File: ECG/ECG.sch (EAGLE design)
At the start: 32 parts, among them J1 TC2030-CTX-NL, U1 BGM111-VISUAL-A, U2 AD8232

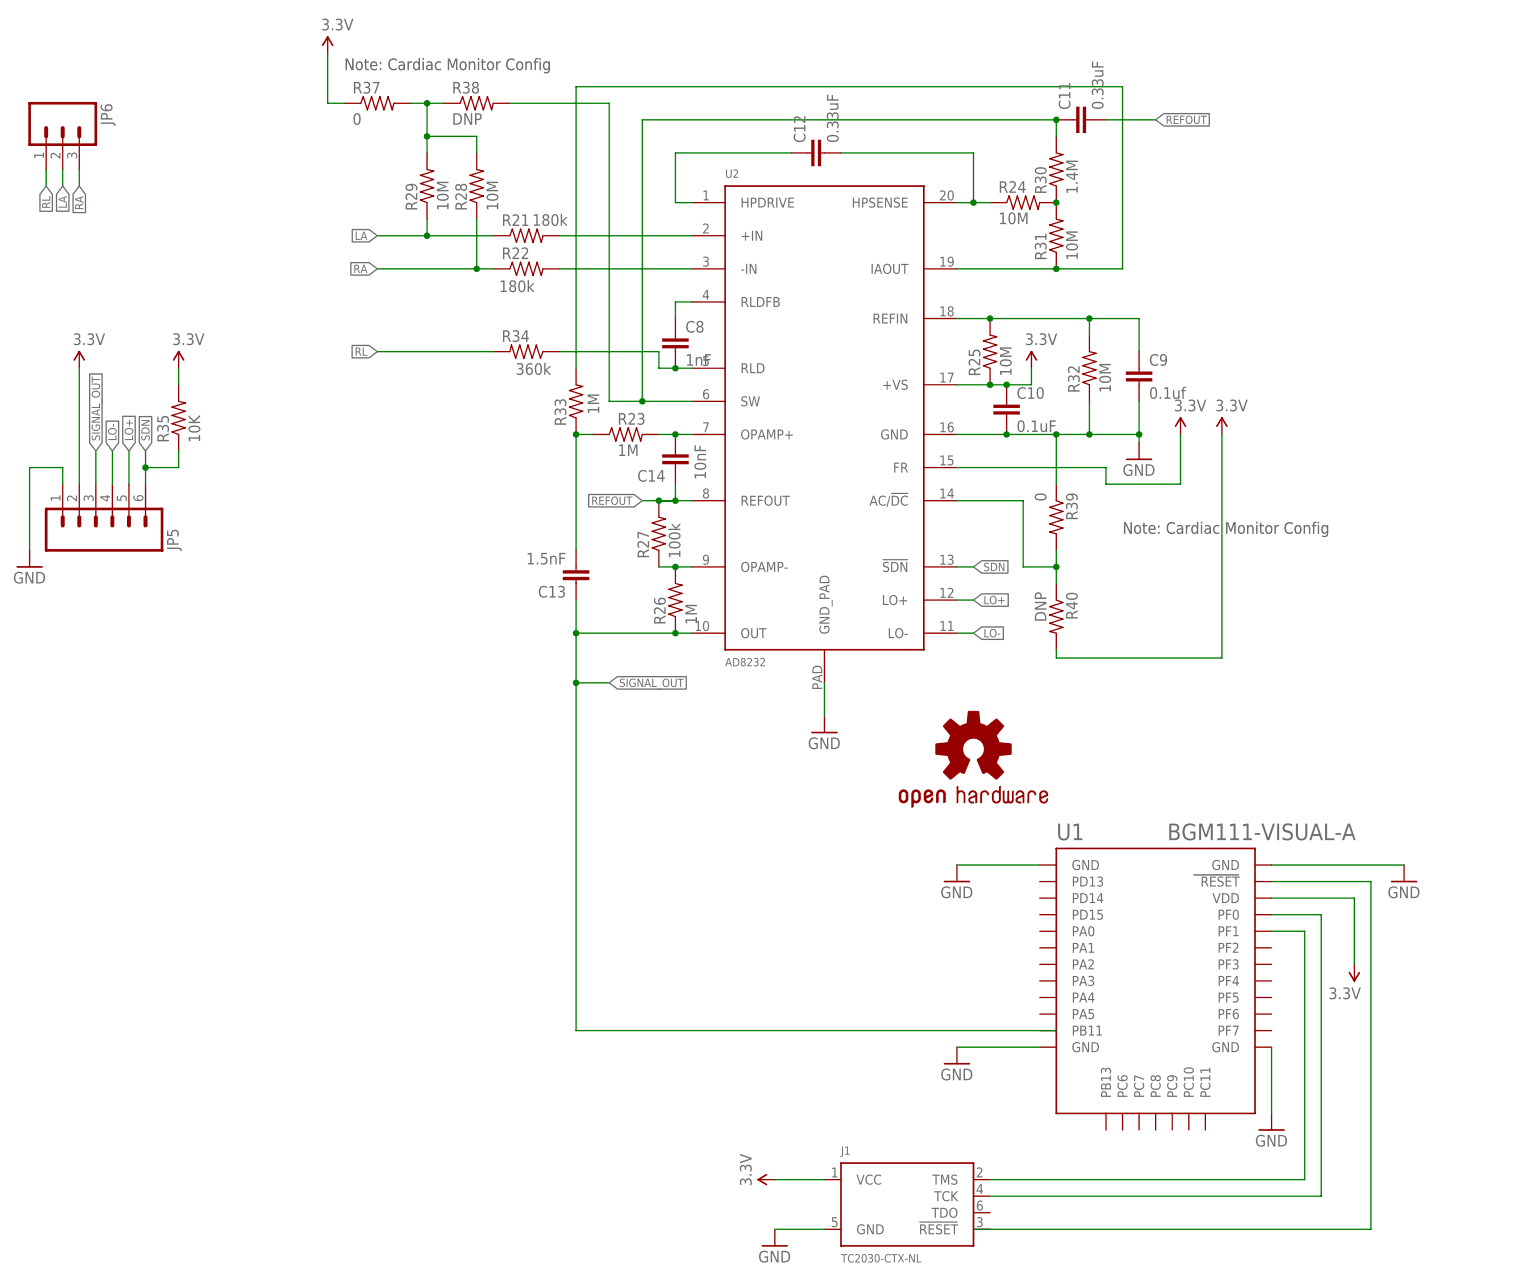
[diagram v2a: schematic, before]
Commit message: Added Batteryholder and snap connectors for RA,LA
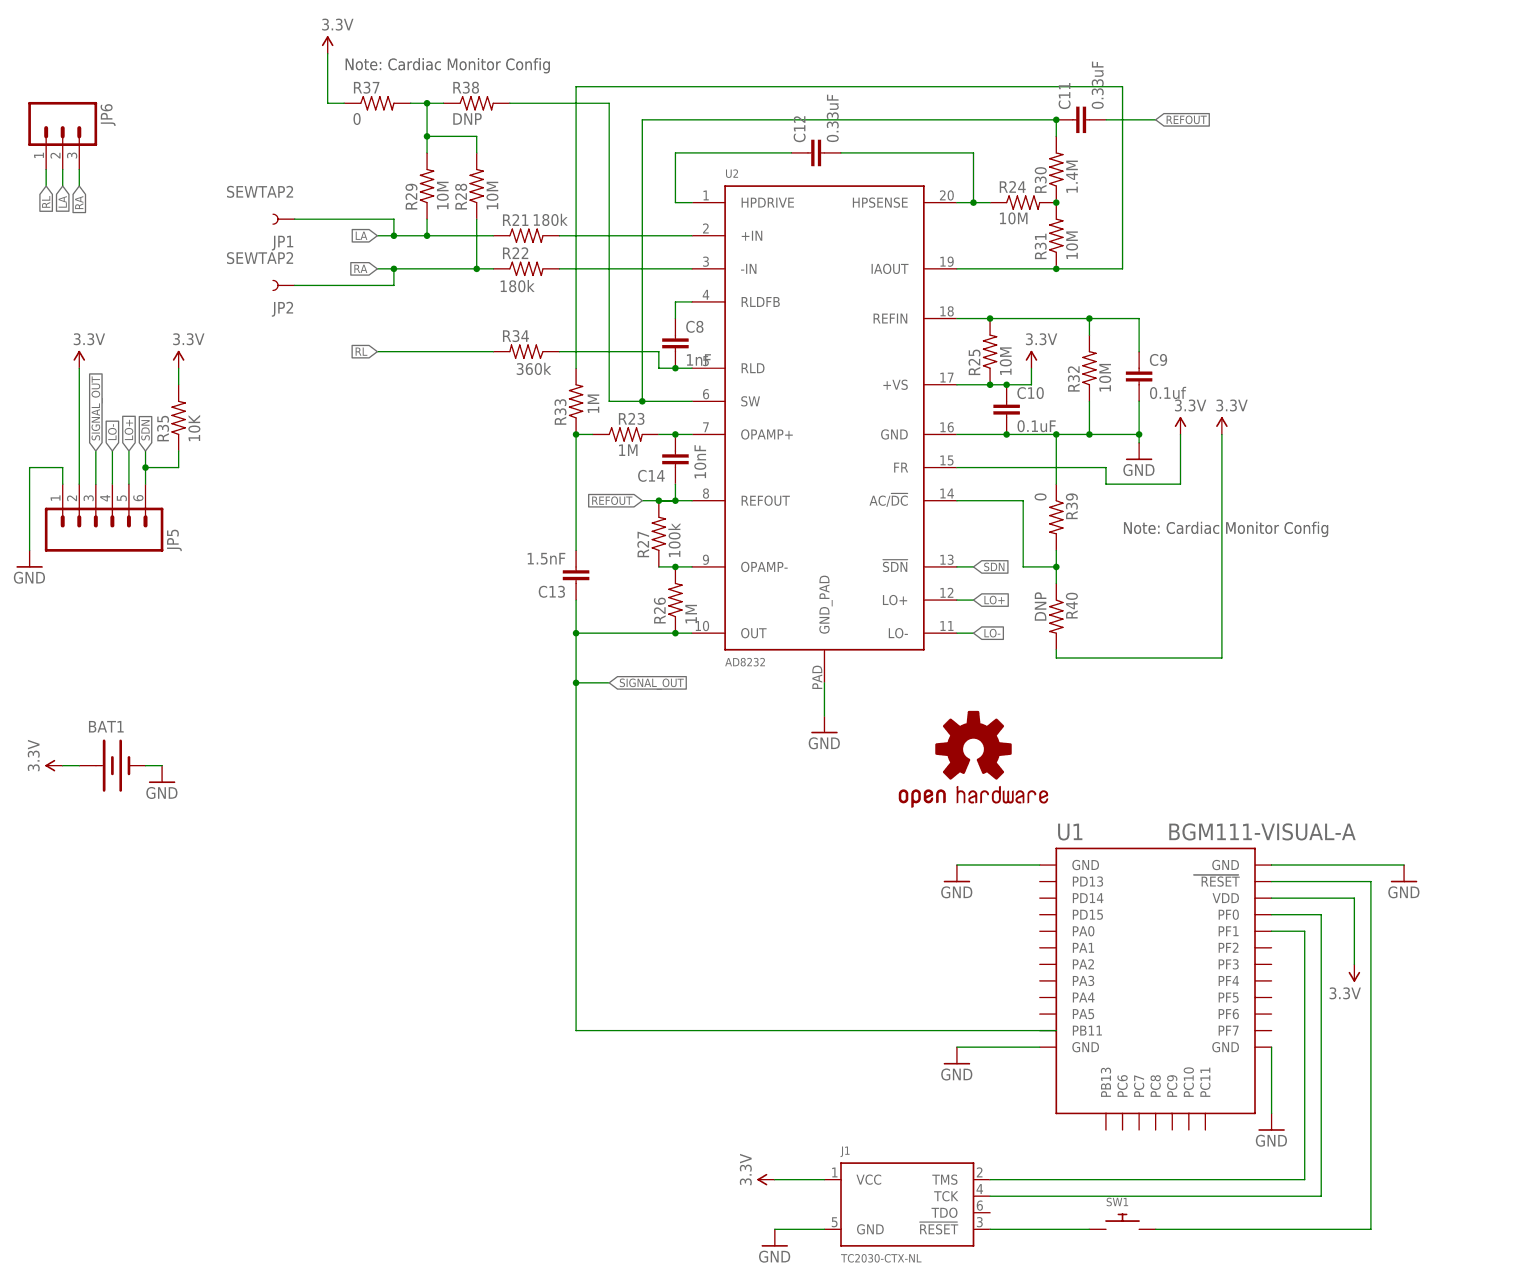
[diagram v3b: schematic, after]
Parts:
- added BAT1: (no value), SparkFun-Electromechanical:BATTERY20SMD
- added JP1, JP2: SEWTAP2, LilyPad-Wearables:SEWTAP2
- added SW1: (no value), adafruit:SWITCH_PUSHBUTTONSOFTTOUCHSMD_SJ
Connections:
- new net N$1: J1.!RESET, SW1.P$1
- net 3.3V: now also BAT1.+
- net GND: now also BAT1.-
- net LA: now also JP1.1
- net N$2: now also SW1.P$2
- net RA: now also JP2.1
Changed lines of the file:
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@@
 <part name="J1" library="tag_connector" deviceset="TC2030-CTX" device="-NL"/>
 <part name="SUPPLY1" library="SparkFun-Aesthetics" deviceset="3.3V" device=""/>
+<part name="BAT1" library="SparkFun-Electromechanical" deviceset="BATTERY" device="20SMD"/>
+<part name="GND9" library="SparkFun-Aesthetics" deviceset="GND" device=""/>
+<part name="SUPPLY3" library="SparkFun-Aesthetics" deviceset="3.3V" device=""/>
+<part name="JP1" library="LilyPad-Wearables" deviceset="SEWTAP" device="2"/>
+<part name="JP2" library="LilyPad-Wearables" deviceset="SEWTAP" device="2"/>
+<part name="SW1" library="adafruit" deviceset="SWITCH_PUSHBUTTON" device="SOFTTOUCHSMD_SJ"/>
 </parts>
 <sheets>
@@
 <instance part="J1" gate="G$1" x="139.7" y="-109.22"/>
 <instance part="SUPPLY1" gate="G$1" x="119.38" y="-106.68" rot="R90"/>
+<instance part="BAT1" gate="G$1" x="17.78" y="-43.18"/>
+<instance part="GND9" gate="1" x="25.4" y="-45.72"/>
+<instance part="SUPPLY3" gate="G$1" x="10.16" y="-43.18" rot="R90"/>
+<instance part="JP1" gate="G$1" x="43.18" y="40.64" rot="R180"/>
+<instance part="JP2" gate="G$1" x="43.18" y="30.48" rot="R180"/>
+<instance part="SW1" gate="G$1" x="172.72" y="-114.3"/>
 </instances>
 <busses>
@@
 <wire x1="119.38" y1="-114.3" x2="127" y2="-114.3" width="0.1524" layer="91"/>
 </segment>
+<segment>
+<pinref part="BAT1" gate="G$1" pin="-"/>
+<pinref part="GND9" gate="1" pin="GND"/>
+<wire x1="22.86" y1="-43.18" x2="25.4" y2="-43.18" width="0.1524" layer="91"/>
+</segment>
 </net>
 <net name="N$12" class="0">
@@
 <wire x1="76.2" y1="38.1" x2="66.04" y2="38.1" width="0.1524" layer="91"/>
 <pinref part="R29" gate="G$1" pin="1"/>
-<wire x1="66.04" y1="38.1" x2="58.42" y2="38.1" width="0.1524" layer="91"/>
+<wire x1="66.04" y1="38.1" x2="60.96" y2="38.1" width="0.1524" layer="91"/>
+<wire x1="60.96" y1="38.1" x2="58.42" y2="38.1" width="0.1524" layer="91"/>
 <wire x1="66.04" y1="40.64" x2="66.04" y2="38.1" width="0.1524" layer="91"/>
 <junction x="66.04" y="38.1"/>
 <label x="58.42" y="38.1" size="1.27" layer="95" rot="R180" xref="yes"/>
+<pinref part="JP1" gate="G$1" pin="1"/>
+<wire x1="45.72" y1="40.64" x2="60.96" y2="40.64" width="0.1524" layer="91"/>
+<wire x1="60.96" y1="40.64" x2="60.96" y2="38.1" width="0.1524" layer="91"/>
+<junction x="60.96" y="38.1"/>
 </segment>
 <segment>
@@
 <wire x1="76.2" y1="33.02" x2="73.66" y2="33.02" width="0.1524" layer="91"/>
 <pinref part="R28" gate="G$1" pin="1"/>
-<wire x1="73.66" y1="33.02" x2="58.42" y2="33.02" width="0.1524" layer="91"/>
+<wire x1="73.66" y1="33.02" x2="60.96" y2="33.02" width="0.1524" layer="91"/>
+<wire x1="60.96" y1="33.02" x2="58.42" y2="33.02" width="0.1524" layer="91"/>
 <wire x1="73.66" y1="40.64" x2="73.66" y2="33.02" width="0.1524" layer="91"/>
 <junction x="73.66" y="33.02"/>
 <label x="58.42" y="33.02" size="1.27" layer="95" rot="R180" xref="yes"/>
+<pinref part="JP2" gate="G$1" pin="1"/>
+<wire x1="45.72" y1="30.48" x2="60.96" y2="30.48" width="0.1524" layer="91"/>
+<wire x1="60.96" y1="30.48" x2="60.96" y2="33.02" width="0.1524" layer="91"/>
+<junction x="60.96" y="33.02"/>
 </segment>
 <segment>
@@
 <pinref part="SUPPLY2" gate="G$1" pin="3.3V"/>
 </segment>
+<segment>
+<pinref part="SUPPLY3" gate="G$1" pin="3.3V"/>
+<pinref part="BAT1" gate="G$1" pin="+"/>
+<wire x1="10.16" y1="-43.18" x2="12.7" y2="-43.18" width="0.1524" layer="91"/>
+</segment>
 </net>
 <net name="LO+" class="0">
@@
 </segment>
 </net>
+<net name="N$1" class="0">
+<segment>
+<pinref part="J1" gate="G$1" pin="!RESET"/>
+<pinref part="SW1" gate="G$1" pin="P$1"/>
+<wire x1="152.4" y1="-114.3" x2="167.64" y2="-114.3" width="0.1524" layer="91"/>
+</segment>
+</net>
 <net name="N$2" class="0">
 <segment>
+<pinref part="SW1" gate="G$1" pin="P$2"/>
+<wire x1="177.8" y1="-114.3" x2="210.82" y2="-114.3" width="0.1524" layer="91"/>
+<wire x1="210.82" y1="-114.3" x2="210.82" y2="-60.96" width="0.1524" layer="91"/>
+<wire x1="210.82" y1="-60.96" x2="195.58" y2="-60.96" width="0.1524" layer="91"/>
 <pinref part="U1" gate="G$1" pin="RESET"/>
-<wire x1="195.58" y1="-60.96" x2="210.82" y2="-60.96" width="0.1524" layer="91"/>
-<wire x1="210.82" y1="-60.96" x2="210.82" y2="-114.3" width="0.1524" layer="91"/>
-<wire x1="210.82" y1="-114.3" x2="149.86" y2="-114.3" width="0.1524" layer="91"/>
-</segment>
-</net>
+</segment>
+</net>
